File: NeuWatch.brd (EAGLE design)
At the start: 43.2 x 40.6 mm, 61 parts, among them IC1 SAMD21G18A-AUT, IC3 TPS2115, IC4 SIP32401A, IC5 MC74VHC1G14DFT, Y1 32,768Khz

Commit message: added batsense
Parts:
- added C2: 100pf, AtomTech:C0402
- added C20: 100nf, AtomTech:C0402
- added R20: 1k, rcl:R0402
- added R21: 560k, rcl:R0402
- added R22: 47k, rcl:R0402
- added R23: 150k, rcl:R0402
- added R24: 5.6k, rcl:R0402
- added T1: (no value), transistor:SOT23-BEC
- added T2: 2N7002_ALT, AtomTech:MOSFET
- moved C18 9.84 mm to (17.7, 2.60)
- moved L3 8.95 mm to (10.7, 13.2)
- moved R17 8.95 mm to (7.18, 10.9)
- moved BOOST 8.95 mm to (10.8, 10.1)
- moved R18 8.95 mm to (14.2, 9.53)
- moved R19 8.95 mm to (14.2, 12.3)
- moved C17 0.89 mm to (14.2, 15.1), turned to 270 degrees
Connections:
- new net N$14: R22.2, T2.S
- new net N$5: C2.2, R21.1, T1.C, T2.G
- new net N$8: R24.1, T1.B
- new net N$9: C2.1, C20.1, R20.1, R21.2, T2.D
- net GND: now also C20.2, R23.1, T1.E
- net PA04_AIN4: now also R22.1, R23.2
- net PA05_AIN5: now also R24.2
- net VIN: now also R20.2
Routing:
- net PA05_AIN5: track 0.00 -> 30.2 mm, vias 0 -> 2
- net VIN: track 42.6 -> 59.8 mm, vias 2 -> 3
- net PA04_AIN4: track 0.00 -> 16.1 mm, vias 0 -> 2
- net N$9: track 0.00 -> 8.19 mm
- net VMAIN: track 52.8 -> 58.9 mm, vias 4 -> 5
- net N$5: track 0.00 -> 5.73 mm
- net TARGET_RESET_EDBG: track 16.9 -> 21.2 mm
- net N$14: track 0.00 -> 2.01 mm
- net 5V: track 98.4 -> 100.2 mm
- net N$8: track 0.00 -> 1.66 mm
- net 3.3V: track 206.9 -> 205.6 mm
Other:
- board text removed: "CS1/D6"
- board text removed: "CS2/D10"
- board text removed: "DC/D7"
- board text removed: "MISO"
- board text removed: "MOSI"
- board text removed: "RST/D8"
- board text removed: "SCK"

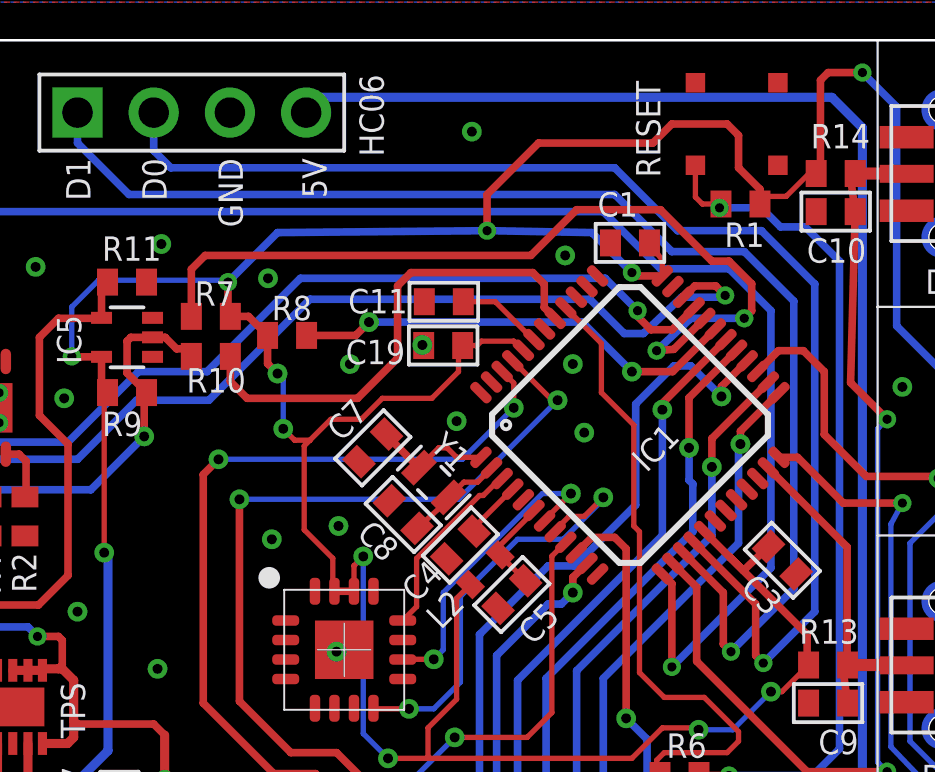
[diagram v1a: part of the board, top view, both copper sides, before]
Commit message: Fixes
I2C removed and resistors for buttons changed.
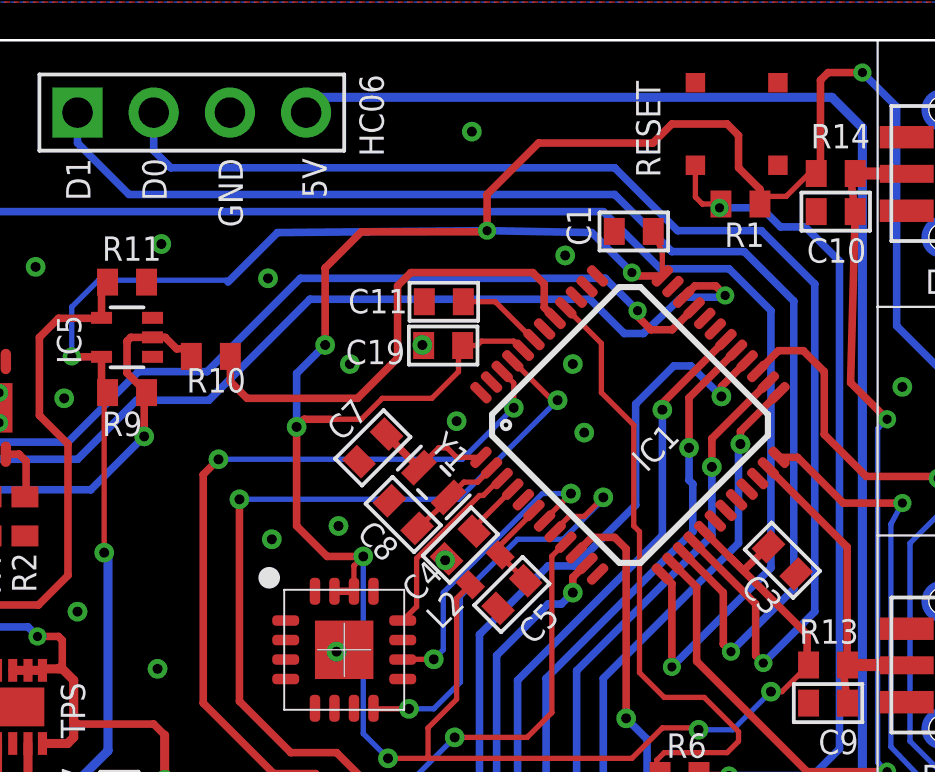
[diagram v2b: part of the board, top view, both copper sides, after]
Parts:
- removed R7, R8: 4.7K, adafruit:R0402
- C10, C15, C16, C9: value (none) -> 100nf
- R13, R14, R15, R16: value (none) -> 47k
- R24: value 5.6k -> 5.6k
- T1: value (none) -> 846
- moved C1 0.40 mm to (31.4, 34.3)
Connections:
- removed net SCL: IC1.32, R7.1
- removed net SDA: IC1.31, R8.1
- net 3.3V: no longer R7.2, R8.2
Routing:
- net SCL: track 28.7 -> 0.00 mm, vias 2 -> 0
- net SDA: track 15.1 -> 0.00 mm, vias 2 -> 0
- net 3.3V: track 205.6 -> 211.1 mm, vias 15 -> 14
- net GND: track 3.27 -> 3.34 mm, vias 25 -> 26

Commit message: via fix
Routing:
- net GND: vias 26 -> 27
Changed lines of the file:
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@@
 <via x="12.827" y="21.59" extent="1-16" drill="0.3302" diameter="0.508"/>
 <via x="11.43" y="33.0835" extent="1-16" drill="0.3302" diameter="0.508"/>
-<via x="7.366" y="10.7315" extent="1-16" drill="0.3302" diameter="0.508"/>
+<via x="7.239" y="9.2075" extent="1-16" drill="0.3302" diameter="0.508"/>
 <via x="1.27" y="26.67" extent="1-16" drill="0.3302" diameter="0.508"/>
 <via x="1.397" y="32.4485" extent="1-16" drill="0.3302" diameter="0.508"/>
@@
 <via x="25.0825" y="23.3045" extent="1-16" drill="0.3302" diameter="0.508"/>
 <wire x1="25.0825" y1="23.3045" x2="25.130878125" y2="23.352878125" width="0.254" layer="1"/>
+<via x="6.4135" y="13.97" extent="1-16" drill="0.3302" diameter="0.508"/>
 </signal>
 <signal name="RESET">
@@
 <contactref element="SWD" pad="10"/>
 <contactref element="RESET" pad="P$3"/>
-<wire x1="33.423" y1="36.471" x2="33.423" y2="35.411" width="0.1778" layer="1"/>
-<wire x1="33.423" y1="35.411" x2="33.655" y2="35.179" width="0.1778" layer="1"/>
-<wire x1="33.655" y1="35.179" x2="34.275" y2="35.179" width="0.1778" layer="1"/>
 <wire x1="34.275" y1="35.179" x2="34.2265" y2="35.1155" width="0.254" layer="1"/>
 <wire x1="34.2265" y1="35.1155" x2="34.2265" y2="35.052" width="0.254" layer="1"/>
@@
 <wire x1="33.4645" y1="15.113" x2="33.4645" y2="16.0505" width="0.254" layer="1"/>
 <wire x1="33.4645" y1="16.0505" x2="33.543" y2="16.129" width="0.254" layer="1"/>
+<wire x1="33.423" y1="36.471" x2="33.423" y2="35.8555" width="0.254" layer="1"/>
+<wire x1="33.423" y1="35.8555" x2="34.2265" y2="35.052" width="0.254" layer="1"/>
 </signal>
 <signal name="SCK/D13">
